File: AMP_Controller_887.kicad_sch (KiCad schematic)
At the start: 65 parts, among them J1 Conn_PIC_ICSP_ICD, J3 4P_I2C, J4 Conn_01x13_Socket, J5 Conn_01x13_Socket, J6 2P_POWER, J7 USB_Mini_B_90_Angled, SW1 SW_RST, SW2 SW_PR21, X1 16MHz

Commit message: Finished layout.
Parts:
- J4, J5: footprint Connector_PinSocket_2.54mm:PinSocket_1x13_P2.54mm_Vertical -> Connector_PinSocket_2.54mm:PinSocket_1x14_P2.54mm_Vertical; symbol Connector:Conn_01x13_Socket -> Connector:Conn_01x14_Socket
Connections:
- net GND: now also J4.14 (Pin_14), J5.14 (Pin_14)
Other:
- moved on the sheet: C10, C11, C12, C13, C14, C7, C9, R10, R11, R12, R13, R14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

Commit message: Swap position of S5/S4 (aka: RX/TX) downward
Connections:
- net GND: now also J5.12 (Pin_12); no longer J5.14 (Pin_14)
- net at R33.1: now also J5.13 (Pin_13); no longer J5.12 (Pin_12)
- net at R34.1: now also J5.14 (Pin_14); no longer J5.13 (Pin_13)
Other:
- moved on the sheet: R33, R34
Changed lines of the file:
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@@
 	(wire
 		(pts
+			(xy 236.22 130.81) (xy 238.76 130.81)
+		)
+		(stroke
+			(width 0)
+			(type default)
+		)
+	)
+	(wire
+		(pts
 			(xy 68.58 175.26) (xy 68.58 166.37)
 		)
@@
 	(wire
 		(pts
+			(xy 236.22 133.35) (xy 238.76 133.35)
+		)
+		(stroke
+			(width 0)
+			(type default)
+		)
+	)
+	(wire
+		(pts
 			(xy 128.27 54.61) (xy 133.35 54.61)
 		)
@@
 	(wire
 		(pts
-			(xy 93.98 130.81) (xy 93.98 156.21)
+			(xy 186.69 133.35) (xy 228.6 133.35)
 		)
 		(stroke
@@
 	(wire
 		(pts
-			(xy 193.04 171.45) (xy 195.58 171.45)
+			(xy 93.98 130.81) (xy 93.98 156.21)
 		)
 		(stroke
@@
 	(wire
 		(pts
-			(xy 105.41 34.29) (xy 110.49 34.29)
+			(xy 193.04 171.45) (xy 195.58 171.45)
 		)
 		(stroke
@@
 	(wire
 		(pts
-			(xy 186.69 128.27) (xy 228.6 128.27)
+			(xy 105.41 34.29) (xy 110.49 34.29)
 		)
 		(stroke
@@
 	(wire
 		(pts
-			(xy 186.69 130.81) (xy 228.6 130.81)
-		)
-		(stroke
-			(width 0)
-			(type default)
-		)
-	)
-	(wire
-		(pts
 			(xy 50.8 179.07) (xy 50.8 171.45)
 		)
@@
 	(wire
 		(pts
-			(xy 227.33 161.29) (xy 246.38 161.29)
+			(xy 186.69 130.81) (xy 228.6 130.81)
 		)
 		(stroke
@@
 	(wire
 		(pts
-			(xy 186.69 125.73) (xy 228.6 125.73)
+			(xy 227.33 161.29) (xy 246.38 161.29)
 		)
 		(stroke
@@
 	(wire
 		(pts
-			(xy 57.15 168.91) (xy 62.23 168.91)
+			(xy 186.69 125.73) (xy 228.6 125.73)
 		)
 		(stroke
@@
 	(wire
 		(pts
-			(xy 186.69 105.41) (xy 204.47 105.41)
+			(xy 57.15 168.91) (xy 62.23 168.91)
 		)
 		(stroke
@@
 	(wire
 		(pts
-			(xy 222.25 158.75) (xy 246.38 158.75)
+			(xy 186.69 105.41) (xy 204.47 105.41)
 		)
 		(stroke
@@
 	(wire
 		(pts
-			(xy 123.19 46.99) (xy 123.19 54.61)
+			(xy 222.25 158.75) (xy 246.38 158.75)
 		)
 		(stroke
@@
 	(wire
 		(pts
-			(xy 50.8 171.45) (xy 55.88 171.45)
+			(xy 123.19 46.99) (xy 123.19 54.61)
 		)
 		(stroke
@@
 	(wire
 		(pts
-			(xy 133.35 46.99) (xy 133.35 54.61)
+			(xy 50.8 171.45) (xy 55.88 171.45)
 		)
 		(stroke
@@
 	(wire
 		(pts
-			(xy 236.22 130.81) (xy 238.76 130.81)
+			(xy 133.35 46.99) (xy 133.35 54.61)
 		)
 		(stroke
@@
 		)
 	)
+	(label "SW5"
+		(at 186.69 130.81 0)
+		(effects
+			(font
+				(size 1.27 1.27)
+			)
+			(justify left bottom)
+		)
+	)
 	(label "OSC2"
 		(at 96.52 118.11 0)
@@
 		)
 	)
-	(label "SW5"
-		(at 186.69 128.27 0)
-		(effects
-			(font
-				(size 1.27 1.27)
-			)
-			(justify left bottom)
-		)
-	)
 	(label "MCLR"
 		(at 96.52 105.41 0)
@@
 		)
 	)
-	(label "SW4"
-		(at 186.69 130.81 0)
-		(effects
-			(font
-				(size 1.27 1.27)
-			)
-			(justify left bottom)
-		)
-	)
 	(label "OSC1"
 		(at 63.5 43.18 180)
@@
 		)
 	)
+	(label "SW4"
+		(at 186.69 133.35 0)
+		(effects
+			(font
+				(size 1.27 1.27)
+			)
+			(justify left bottom)
+		)
+	)
 	(label "AN10"
 		(at 165.1 125.73 180)
@@
 	(symbol
 		(lib_id "Device:R_US")
-		(at 232.41 128.27 270)
+		(at 232.41 130.81 270)
 		(unit 1)
 		(exclude_from_sim no)
@@
 		(dnp no)
 		(property "Reference" "R33"
-			(at 234.696 127.254 90)
+			(at 234.696 129.794 90)
 			(effects
 				(font
@@
 		)
 		(property "Value" "1k"
-			(at 226.568 127 90)
+			(at 226.568 129.54 90)
 			(effects
 				(font
@@
 		)
 		(property "Footprint" "Resistor_THT:R_Axial_DIN0204_L3.6mm_D1.6mm_P5.08mm_Horizontal"
-			(at 232.156 129.286 90)
+			(at 232.156 131.826 90)
 			(effects
 				(font
@@
 		)
 		(property "Datasheet" "~"
-			(at 232.41 128.27 0)
+			(at 232.41 130.81 0)
 			(effects
 				(font
@@
 		)
 		(property "Description" "Resistor, US symbol"
-			(at 232.41 128.27 0)
+			(at 232.41 130.81 0)
 			(effects
 				(font
@@
 	(symbol
 		(lib_id "power:GND")
-		(at 238.76 133.35 270)
+		(at 236.22 128.27 270)
 		(unit 1)
 		(exclude_from_sim no)
@@
 		(fields_autoplaced yes)
 		(property "Reference" "#PWR023"
-			(at 232.41 133.35 0)
+			(at 229.87 128.27 0)
 			(effects
 				(font
@@
 		)
 		(property "Value" "GND"
-			(at 234.95 133.3499 90)
+			(at 232.41 128.2699 90)
 			(effects
 				(font
@@
 		)
 		(property "Footprint" ""
-			(at 238.76 133.35 0)
+			(at 236.22 128.27 0)
 			(effects
 				(font
@@
 		)
 		(property "Datasheet" ""
-			(at 238.76 133.35 0)
+			(at 236.22 128.27 0)
 			(effects
 				(font
@@
 		)
 		(property "Description" "Power symbol creates a global label with name \"GND\" , ground"
-			(at 238.76 133.35 0)
+			(at 236.22 128.27 0)
 			(effects
 				(font
@@
 	(symbol
 		(lib_id "Device:R_US")
-		(at 232.41 130.81 270)
+		(at 232.41 133.35 270)
 		(unit 1)
 		(exclude_from_sim no)
@@
 		(dnp no)
 		(property "Reference" "R34"
-			(at 234.696 129.794 90)
+			(at 234.696 132.334 90)
 			(effects
 				(font
@@
 		)
 		(property "Value" "1k"
-			(at 226.568 129.54 90)
+			(at 226.568 132.08 90)
 			(effects
 				(font
@@
 		)
 		(property "Footprint" "Resistor_THT:R_Axial_DIN0204_L3.6mm_D1.6mm_P5.08mm_Horizontal"
-			(at 232.156 131.826 90)
+			(at 232.156 134.366 90)
 			(effects
 				(font
@@
 		)
 		(property "Datasheet" "~"
-			(at 232.41 130.81 0)
+			(at 232.41 133.35 0)
 			(effects
 				(font
@@
 		)
 		(property "Description" "Resistor, US symbol"
-			(at 232.41 130.81 0)
+			(at 232.41 133.35 0)
 			(effects
 				(font

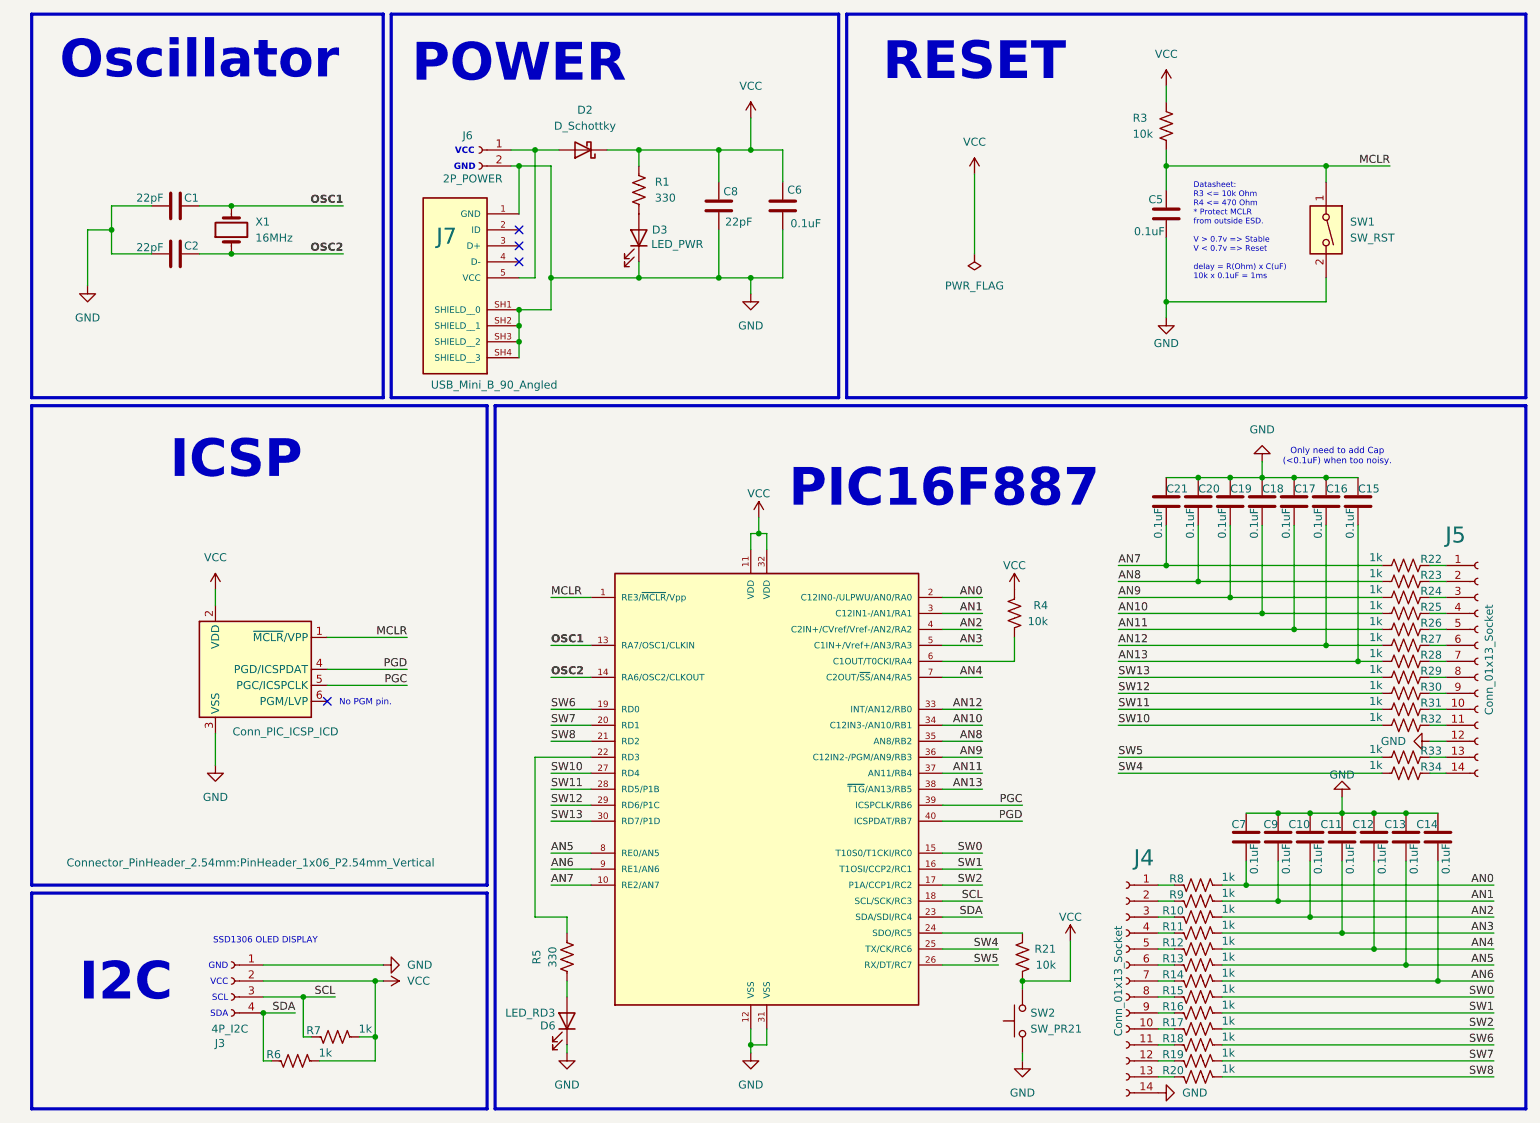
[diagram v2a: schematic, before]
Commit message: Rev.2 : Flip USB to be normal, remove all R/C from I/O, Fix pull-up button, refine fonts.
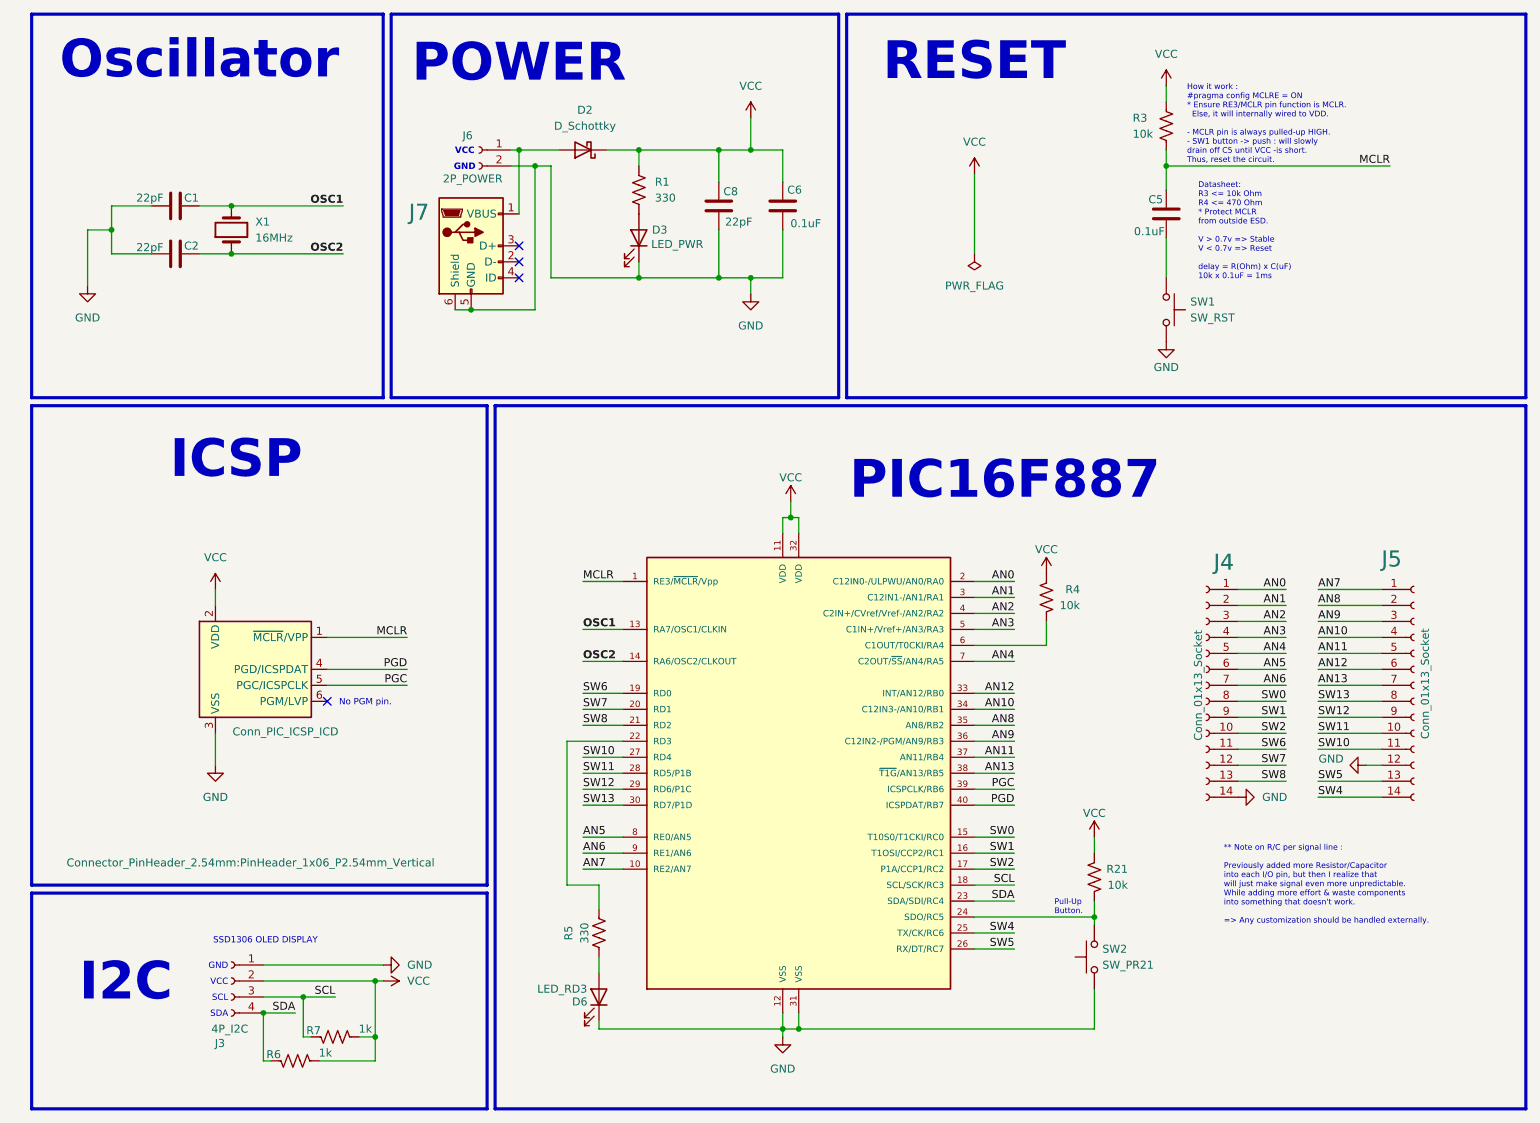
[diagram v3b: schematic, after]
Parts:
- removed C10, C11, C12, C13, C14, C15, C16, C17, C18, C19, C20, C21, C7, C9: 0.1uF, Capacitor_THT:C_Disc_D3.0mm_W1.6mm_P2.50mm, symbol Device:C
- removed R10, R11, R12, R13, R14, R15, R16, R17, R18, R19, R20, R22, R23, R24, R25, R26, R27, R28, R29, R30, R31, R32, R33, R34, R8, R9: 1k, Resistor_THT:R_Axial_DIN0204_L3.6mm_D1.6mm_P5.08mm_Horizontal, symbol Device:R_US
- J7: footprint Connector:USB_MINI_B_90_Angled -> Connector_USB:USB_MINI_B_90_Angled; symbol Connector:USB_Mini_B_90_Angled -> Connector:USB_B_Mini
- SW1: symbol Switch:SW_DIP_x01 -> Switch:SW_Push
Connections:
- net AN0: now also J4.1 (Pin_1)
- net AN1: now also J4.2 (Pin_2)
- net AN10: now also J5.4 (Pin_4)
- net AN11: now also J5.5 (Pin_5)
- net AN12: now also J5.6 (Pin_6)
- net AN13: now also J5.7 (Pin_7)
- net AN2: now also J4.3 (Pin_3)
- net AN3: now also J4.4 (Pin_4)
- net AN4: now also J4.5 (Pin_5)
- net AN5: now also J4.6 (Pin_6)
- net AN6: now also J4.7 (Pin_7)
- net AN7: now also J5.1 (Pin_1)
- net AN8: now also J5.2 (Pin_2)
- net AN9: now also J5.3 (Pin_3)
- net GND: now also J7.5 (GND), J7.6 (Shield); no longer C5.1, J7.1 (GND), J7.SH1 (SHIELD__0), J7.SH2 (SHIELD__1), J7.SH3 (SHIELD__2), J7.SH4 (SHIELD__3)
- net MCLR: no longer SW1.1
- net SW0: now also J4.8 (Pin_8)
- net SW1: now also J4.9 (Pin_9)
- net SW10: now also J5.11 (Pin_11)
- net SW11: now also J5.10 (Pin_10)
- net SW12: now also J5.9 (Pin_9)
- net SW13: now also J5.8 (Pin_8)
- net SW2: now also J4.10 (Pin_10)
- net SW4: now also J5.14 (Pin_14)
- net SW5: now also J5.13 (Pin_13)
- net SW6: now also J4.11 (Pin_11)
- net SW7: now also J4.12 (Pin_12)
- net SW8: now also J4.13 (Pin_13)
- net VCC: now also R21.1; no longer R21.2, SW2.2
- net at D2.2 (A), J6.1 (Pin_1): now also J7.1 (VBUS); no longer J7.5 (VCC)
- net at PIC16F887.24 (SDO/RC5): now also R21.2, SW2.2; no longer R21.1
- new net: C5.1, SW1.1
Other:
- note added: "** Note on R/C per signal line : Previously added more Resistor/Capacitor into each I/O pin, but then I realize that will just make signal even more unpredictable. While adding more effort & waste components into something that doesn't work. => Any customization should be handled externally."
- note added: "How it work : #pragma config MCLRE = ON * Ensure RE3/MCLR pin function is MCLR. Else, it will internally wired to VDD. - MCLR pin is always pulled-up HIGH. - SW1 button -> push : will slowly drain off C5 until VCC -is short. Thus, reset the circuit."
- note added: "Pull-Up Button."
- note removed: "Only need to add Cap (<0.1uF) when too noisy."
- moved on the sheet: D6, J4, J5, R21, R4, R5, SW2
